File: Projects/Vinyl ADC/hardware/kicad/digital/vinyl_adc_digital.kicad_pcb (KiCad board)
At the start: 2 copper layers, 100 x 100 mm, 17 parts, among them J1 CLK SEL, J2 TO PI GPIO, J4 2x8 BUS, U3 74HCT132, U4 74HC4040, U6 74HC157, U8 74HC4049, X1 6.144MHz

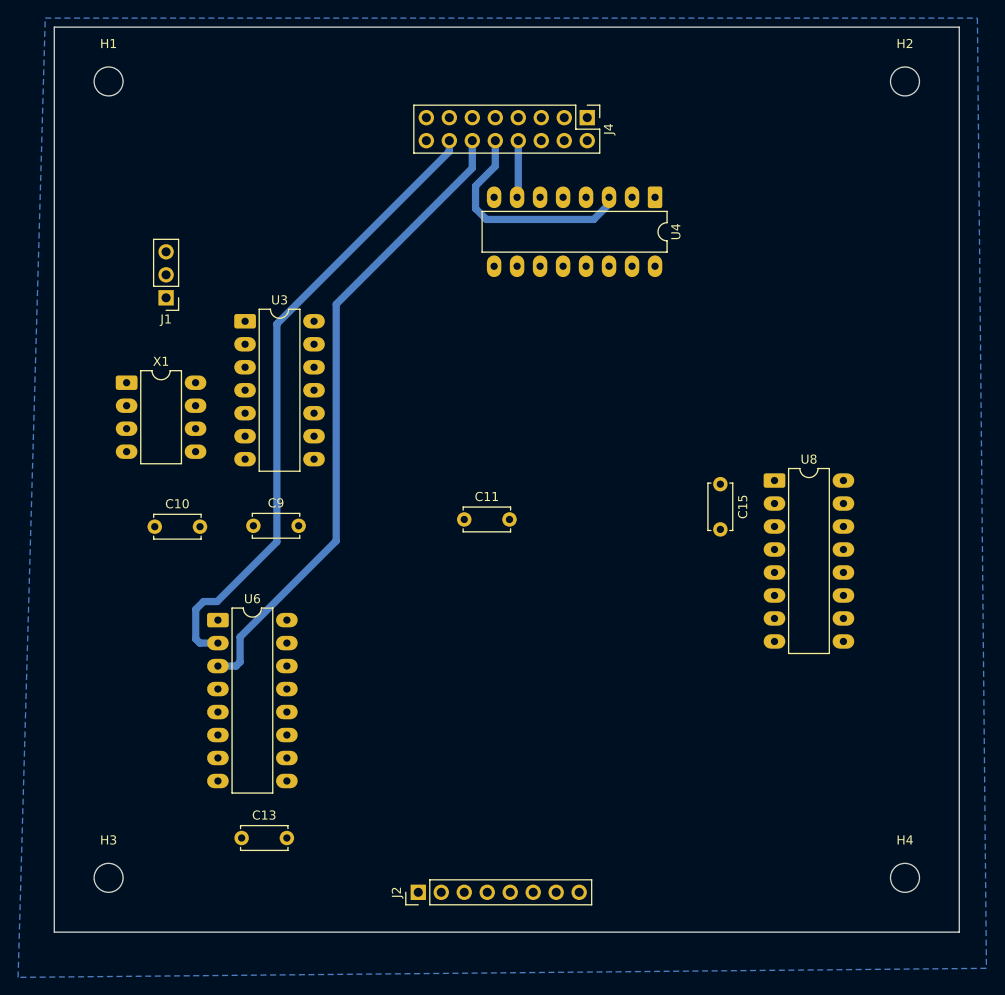
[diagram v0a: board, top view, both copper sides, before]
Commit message: Vinyl ADC: cut the channel double-sided, restore the DRC rules
The three boards were unjudgeable: a previous rebuild deleted every
.kicad_dru, so all three reported bare clearance errors with no way to
tell a real one from the documented exception. Restore them per the
memberOfFootprint recipe -- all 116 hits turn out to be intra-footprint
pad-to-pad at 0.840 mm against the 0.85 mm rule, on fixed 2.54 mm header
pitch, and not one of them was real. The rules do override the board
minimum in KiCad 10; checked rather than assumed.

Netclass was 0.5/0.6 on all three, below the boards' own 0.85/0.8 minima,
so anything that routed them would have laid copper the mill cannot cut.

The channel artwork is now DOUBLE-SIDED -- it is the one milled twice, and
it gets the two pieces of double-sided stock. Its ground was genuinely
broken before this: 32 GND pads in two electrically separate pieces, 30
pour fragments, 24 pads that could only get home through a track, and nine
wire bridges. That fault would have shipped twice. It is now one whole
plane, no stranded pads, zero vias, and one link left.

Four architectures were measured on the same placement before picking one:

  signals on top, GND plane below   6 links, 0 vias, plane whole    91 top joints
  both layers, GND poured           2 links, 1 via,  plane in 3     55 top joints
  leftovers on top  <- shipped      1 link,  0 vias, plane whole    20 top joints

An open link is a wire, and a wire is soldered at both ends -- the same two
joints a milled top-side trace between those pads needs. So moving only the
leftovers to the top costs nothing to build and removes the wire. The full
re-routes buy a prettier plane for 35-71 extra joints, most under sockets.

Registration for the flip is already in the artwork: the four M3 holes sit
at exactly +/-44.00 mm from the board centre in both axes, so the pattern
maps onto itself and two dowels through a diagonal pair are enough.

digital was not routed at all -- 3 of 20 nets, zone u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
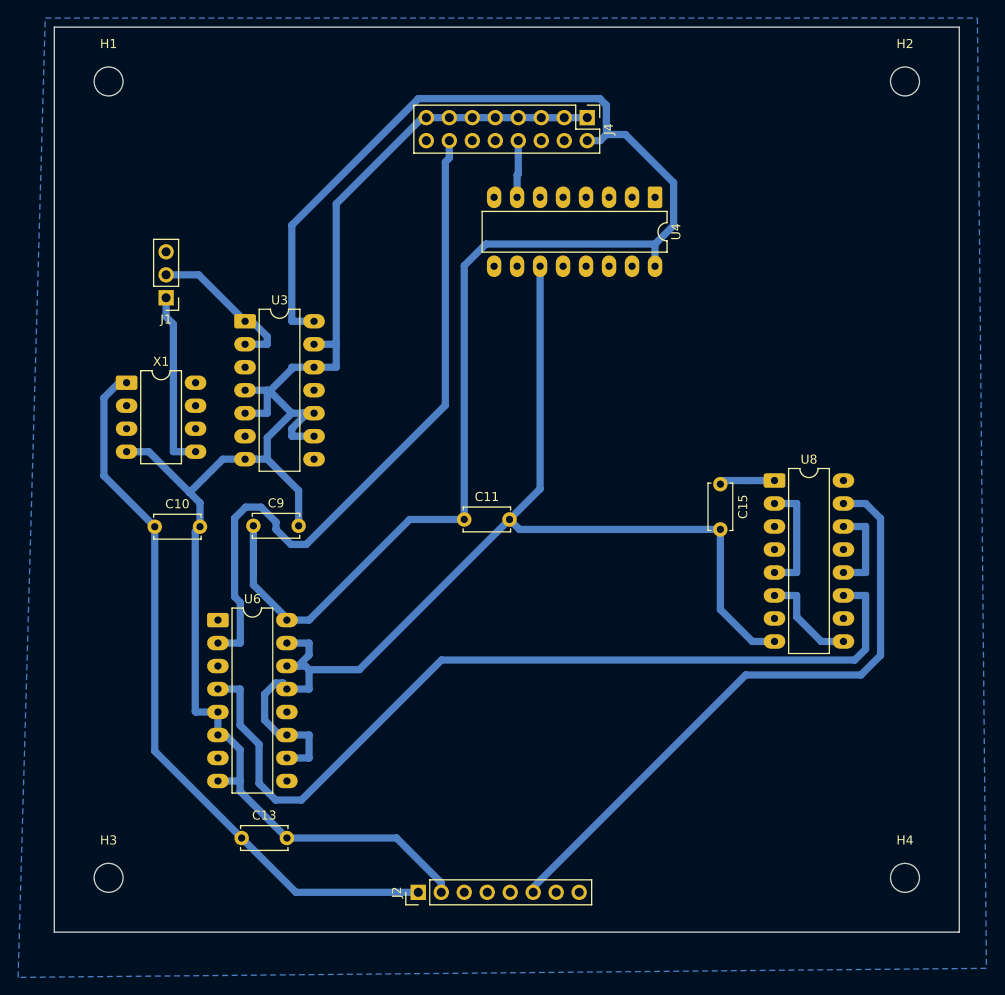
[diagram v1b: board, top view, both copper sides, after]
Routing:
- net GND: track 0.00 -> 309.5 mm
- net +5V: track 0.00 -> 245.8 mm
- net DIN: track 0.00 -> 96.8 mm
- net QL: track 70.9 -> 0.00 mm
- net PI_DIN: track 0.00 -> 69.5 mm
- net PUMP: track 25.1 -> 0.00 mm
- net Net-(J1-Pin_1): track 0.00 -> 19.8 mm
- net Net-(J1-Pin_2): track 0.00 -> 17.3 mm
- net Net-(U8-Pad2): track 0.00 -> 12.5 mm
- net Net-(U8-Pad6): track 0.00 -> 11.1 mm
- net Net-(U8-Pad12): track 0.00 -> 9.98 mm
- net QR: track 70.2 -> 78.3 mm
- net +3V3: track 0.00 -> 6.15 mm

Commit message: Vinyl ADC: the digital and power layouts as fabricated
The two boards milled on 2026-09-03, side by side on one sheet. Editor
history folders are ignored from here on.
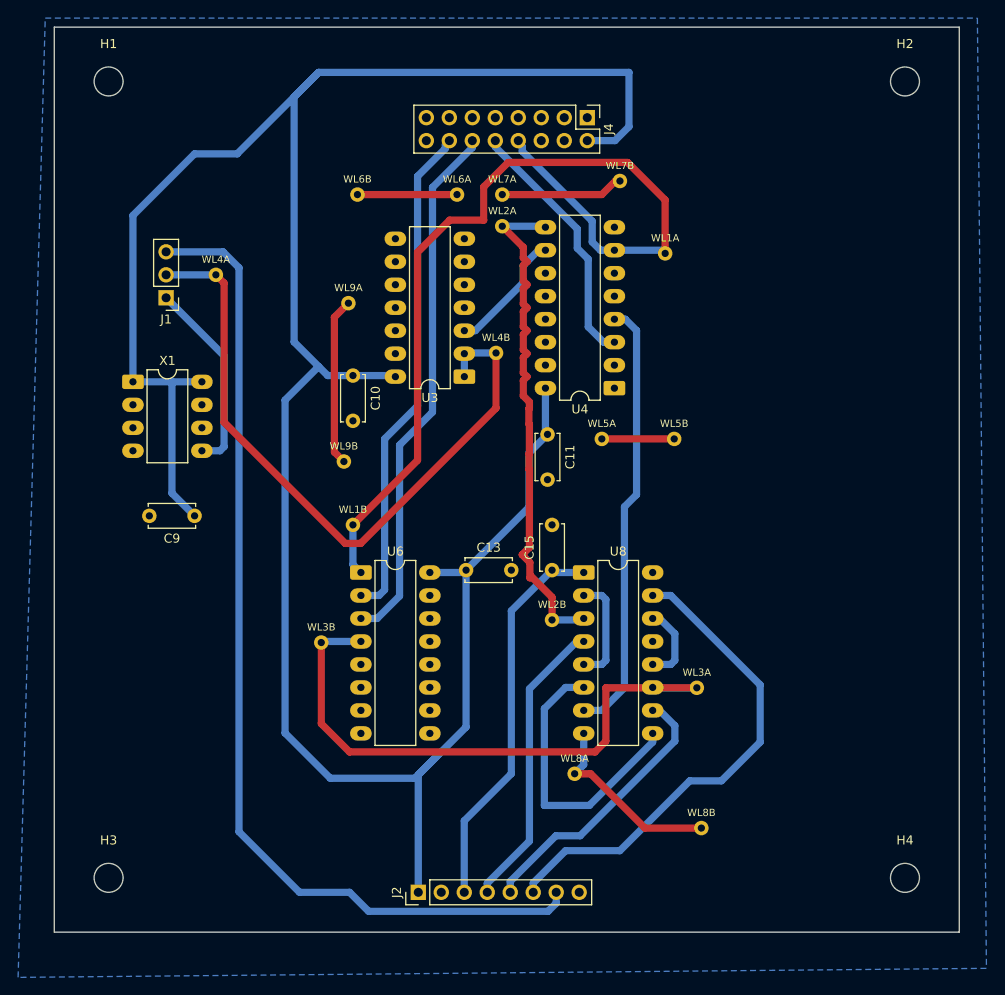
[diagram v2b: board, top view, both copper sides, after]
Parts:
- added WL1A: MCLK, WireLink_TH, F.Cu at (87.5, 45.0)
- added WL1B: MCLK, WireLink_TH, F.Cu at (53.0, 75.0)
- added WL2A: BCLK, WireLink_TH, F.Cu at (69.5, 42.0)
- added WL2B: BCLK, WireLink_TH, F.Cu at (75.0, 85.5)
- added WL3A: DIN, WireLink_TH, F.Cu at (91.0, 93.0)
- added WL3B: DIN, WireLink_TH, F.Cu at (49.5, 88.0)
- added WL4A: Net-(J1-Pin_2), WireLink_TH, F.Cu at (37.9, 47.4)
- added WL4B: Net-(J1-Pin_2), WireLink_TH, F.Cu at (68.8, 56.0)
- added WL5A: GND, WireLink_TH, F.Cu at (80.5, 65.5)
- added WL5B: GND, WireLink_TH, F.Cu at (88.5, 65.5)
- added WL6A: GND, WireLink_TH, F.Cu at (64.5, 38.5)
- added WL6B: GND, WireLink_TH, F.Cu at (53.5, 38.5)
- added WL7A: GND, WireLink_TH, F.Cu at (69.5, 38.5)
- added WL7B: GND, WireLink_TH, F.Cu at (82.5, 37.0)
- added WL8A: GND, WireLink_TH, F.Cu at (77.5, 102.5)
- added WL8B: GND, WireLink_TH, F.Cu at (91.5, 108.5)
- added WL9A: GND, WireLink_TH, F.Cu at (52.5, 50.5)
- added WL9B: GND, WireLink_TH, F.Cu at (52.0, 68.0)
- moved C13 38.6 mm to (65.5, 80.0)
- moved C10 27.5 mm to (53.0, 58.5), turned to -90 degrees
- moved U3 25.0 mm to (65.3, 58.6), turned to 180 degrees
- moved U8 23.4 mm to (78.5, 80.3)
- moved U4 21.6 mm to (81.9, 59.9), turned to 180 degrees
- moved C15 20.9 mm to (75.0, 80.0), turned to 90 degrees
- moved U6 16.7 mm to (53.9, 80.3)
- moved C11 13.2 mm to (74.5, 65.0), turned to -90 degrees
- moved C9 6.59 mm to (35.5, 74.0), turned to 180 degrees
- moved X1 0.71 mm to (28.7, 59.2)
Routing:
- net GND: track 309.5 -> 72.5 mm
- net GPCLK0: track 0.00 -> 111.4 mm
- net MCLK: track 6.31 -> 103.1 mm
- net QL: track 0.00 -> 58.9 mm
- net Net-(J1-Pin_2): track 17.3 -> 76.1 mm
- net BCLK: track 0.00 -> 57.5 mm
- net LRCLK: track 0.00 -> 48.5 mm
- net +5V: track 245.8 -> 286.5 mm
- net +3V3: track 6.15 -> 43.2 mm
- net PI_BCLK: track 0.00 -> 32.6 mm
- net PI_LRCLK: track 0.00 -> 30.7 mm
- net DIN: track 96.8 -> 67.5 mm
- net PUMP: track 0.00 -> 28.4 mm
- net QR: track 78.3 -> 55.5 mm
- net Net-(U8-Pad6): track 11.1 -> 31.8 mm
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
